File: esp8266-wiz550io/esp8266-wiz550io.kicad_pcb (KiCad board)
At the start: 2 copper layers, 31.8 x 50.8 mm, 25 parts, among them J1 Conn_01x02, J2 Conn_01x04, J3 Conn_01x08, J4 Conn_01x06, J5 Conn_01x02, J6 Conn_01x03, J7 Conn_01x02, U1 ESP-12, U2 M74VHC1GT50DTT1G, U3 AP2112K-3.3

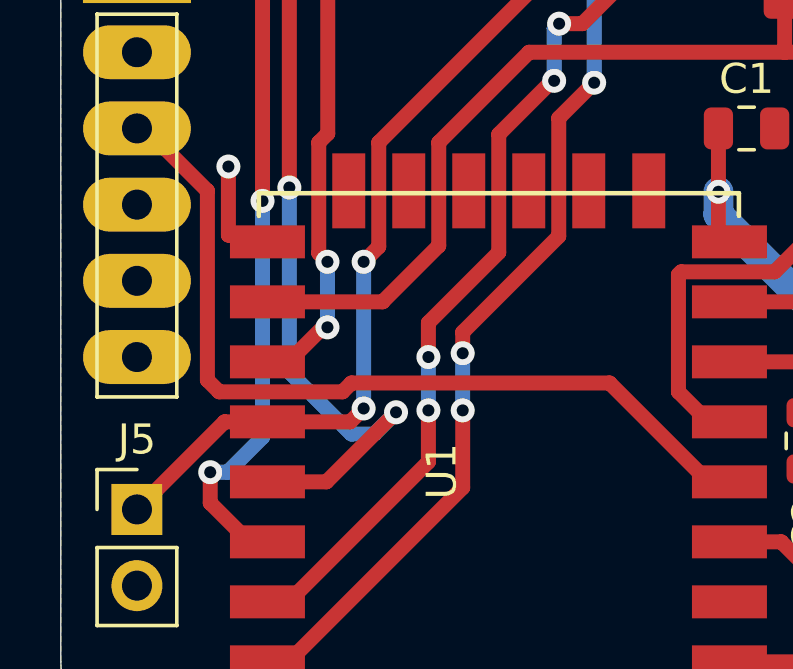
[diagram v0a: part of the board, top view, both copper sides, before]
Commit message: esp8266-wiz550io: switch GPIO2 and GPIO4
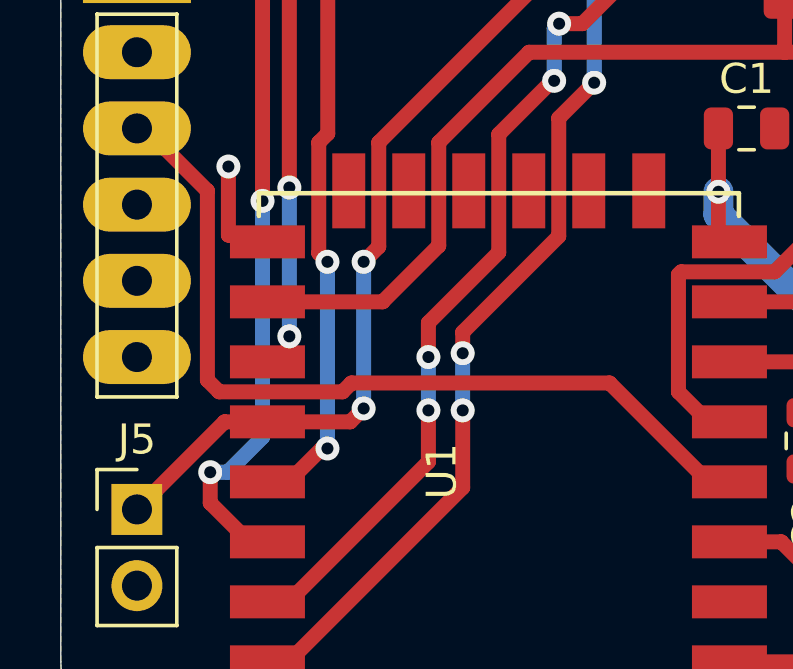
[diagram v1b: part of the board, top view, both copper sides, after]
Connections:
- R4 pad 2: /GPIO4 -> /GPIO2
- U2 pad 2: /GPIO2 -> /GPIO4
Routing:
- net /GPIO4: track 39.8 -> 24.1 mm, vias 4 -> 2
- net /GPIO2: track 20.1 -> 30.2 mm, vias 2 -> 4
